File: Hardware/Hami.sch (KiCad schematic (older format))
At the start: 45 parts, among them J1 OLED, J2 BAT, SW1 Reset, SW10 MX, SW11 MX, SW12 MX, SW13 MX, SW14 MX, SW15 MX, SW16 MX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

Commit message: Hami V1.1
Because who doesn't need rotary encoder support in the botton and top left corners? Also re-routed some of the traces.
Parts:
- added SW20: Rot_1, Rotary_Encoder:RotaryEncoder_Alps_EC11E-Switch_Vertical_H20mm, symbol Device:Rotary_Encoder_Switch
- added SW21: Rot_2, Rotary_Encoder:RotaryEncoder_Alps_EC11E-Switch_Vertical_H20mm, symbol Device:Rotary_Encoder_Switch
- SW10, SW11, SW12, SW13, SW14, SW15, SW16, SW17, SW18, SW19, SW2, SW3, SW4, SW5, SW6, SW7, SW8, SW9: symbol Numpad:MX-NoLED -> Hami:MX-NoLED
- U1: symbol Numpad:ProMicro -> Hami:ProMicro
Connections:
- net labels added: Rot_1A, Rot_1B, Rot_2A, Rot_2B
- net labels removed: GND2
- wire segments 67 -> 76
- no-connect marks 7 -> 5
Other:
- moved on the sheet: D1, D10, D11, D12, D13, D14, D15, D16, D17, D18, D2, D3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

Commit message: Changed footprint references
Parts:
- J1: footprint Numpad:PinHeader_1x04_P2.54mm_Vertical_No_Silk -> Hami:PinHeader_1x04_P2.54mm_Vertical_No_Silk
- J2: footprint Numpad:Battery_Solder_Points -> Hami:Battery_Solder_Points
- SW10, SW11, SW12, SW13, SW14, SW15, SW16, SW17, SW2, SW3, SW4, SW5, SW6, SW7, SW8, SW9: footprint Numpad:CherryMX_Hotswap_SMK -> Hami:CherryMX_Hotswap_SMK
- SW18, SW19: footprint Numpad:CherryMX_Hotswap_2u_SMK -> Hami:CherryMX_Hotswap_2u_SMK
- U1: footprint Numpad:ArduinoProMicro_Blank -> Hami:ArduinoProMicro_Blank
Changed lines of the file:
@@
 F 0 "SW7" H 6625 1300 50  0000 C CNN
 F 1 "MX" H 6625 850 60  0001 C CNN
-F 2 "Numpad:CherryMX_Hotswap_SMK" H 6625 1150 60  0001 C CNN
+F 2 "Hami:CherryMX_Hotswap_SMK" H 6625 1150 60  0001 C CNN
 F 3 "" H 6625 1150 60  0001 C CNN
 	1    6625 1150
@@
 F 0 "SW12" H 7075 1300 50  0000 C CNN
 F 1 "MX" H 7075 850 60  0001 C CNN
-F 2 "Numpad:CherryMX_Hotswap_SMK" H 7075 1150 60  0001 C CNN
+F 2 "Hami:CherryMX_Hotswap_SMK" H 7075 1150 60  0001 C CNN
 F 3 "" H 7075 1150 60  0001 C CNN
 	1    7075 1150
@@
 F 0 "SW17" H 7575 1300 50  0000 C CNN
 F 1 "MX" H 7575 850 60  0001 C CNN
-F 2 "Numpad:CherryMX_Hotswap_SMK" H 7575 1150 60  0001 C CNN
+F 2 "Hami:CherryMX_Hotswap_SMK" H 7575 1150 60  0001 C CNN
 F 3 "" H 7575 1150 60  0001 C CNN
 	1    7575 1150
@@
 F 0 "SW8" H 6625 1900 50  0000 C CNN
 F 1 "MX" H 6625 1450 60  0001 C CNN
-F 2 "Numpad:CherryMX_Hotswap_SMK" H 6625 1750 60  0001 C CNN
+F 2 "Hami:CherryMX_Hotswap_SMK" H 6625 1750 60  0001 C CNN
 F 3 "" H 6625 1750 60  0001 C CNN
 	1    6625 1750
@@
 F 0 "SW13" H 7075 1900 50  0000 C CNN
 F 1 "MX" H 7075 1450 60  0001 C CNN
-F 2 "Numpad:CherryMX_Hotswap_SMK" H 7075 1750 60  0001 C CNN
+F 2 "Hami:CherryMX_Hotswap_SMK" H 7075 1750 60  0001 C CNN
 F 3 "" H 7075 1750 60  0001 C CNN
 	1    7075 1750
@@
 F 0 "SW9" H 6625 2500 50  0000 C CNN
 F 1 "MX" H 6625 2050 60  0001 C CNN
-F 2 "Numpad:CherryMX_Hotswap_SMK" H 6625 2350 60  0001 C CNN
+F 2 "Hami:CherryMX_Hotswap_SMK" H 6625 2350 60  0001 C CNN
 F 3 "" H 6625 2350 60  0001 C CNN
 	1    6625 2350
@@
 F 0 "SW14" H 7075 2500 50  0000 C CNN
 F 1 "MX" H 7075 2050 60  0001 C CNN
-F 2 "Numpad:CherryMX_Hotswap_SMK" H 7075 2350 60  0001 C CNN
+F 2 "Hami:CherryMX_Hotswap_SMK" H 7075 2350 60  0001 C CNN
 F 3 "" H 7075 2350 60  0001 C CNN
 	1    7075 2350
@@
 F 0 "SW10" H 6625 3100 50  0000 C CNN
 F 1 "MX" H 6625 2650 60  0001 C CNN
-F 2 "Numpad:CherryMX_Hotswap_SMK" H 6625 2950 60  0001 C CNN
+F 2 "Hami:CherryMX_Hotswap_SMK" H 6625 2950 60  0001 C CNN
 F 3 "" H 6625 2950 60  0001 C CNN
 	1    6625 2950
@@
 F 0 "SW15" H 7075 3100 50  0000 C CNN
 F 1 "MX" H 7075 2650 60  0001 C CNN
-F 2 "Numpad:CherryMX_Hotswap_SMK" H 7075 2950 60  0001 C CNN
+F 2 "Hami:CherryMX_Hotswap_SMK" H 7075 2950 60  0001 C CNN
 F 3 "" H 7075 2950 60  0001 C CNN
 	1    7075 2950
@@
 F 0 "SW16" H 7075 3700 50  0000 C CNN
 F 1 "MX" H 7075 3250 60  0001 C CNN
-F 2 "Numpad:CherryMX_Hotswap_SMK" H 7075 3550 60  0001 C CNN
+F 2 "Hami:CherryMX_Hotswap_SMK" H 7075 3550 60  0001 C CNN
 F 3 "" H 7075 3550 60  0001 C CNN
 	1    7075 3550
@@
 F 0 "SW18" H 7575 2500 50  0000 C CNN
 F 1 "MX" H 7575 2050 60  0001 C CNN
-F 2 "Numpad:CherryMX_Hotswap_2u_SMK" H 7575 2350 60  0001 C CNN
+F 2 "Hami:CherryMX_Hotswap_2u_SMK" H 7575 2350 60  0001 C CNN
 F 3 "" H 7575 2350 60  0001 C CNN
 	1    7575 2350
@@
 F 0 "SW19" H 7575 3700 50  0000 C CNN
 F 1 "MX" H 7575 3250 60  0001 C CNN
-F 2 "Numpad:CherryMX_Hotswap_2u_SMK" H 7575 3550 60  0001 C CNN
+F 2 "Hami:CherryMX_Hotswap_2u_SMK" H 7575 3550 60  0001 C CNN
 F 3 "" H 7575 3550 60  0001 C CNN
 	1    7575 3550
@@
 F 0 "SW2" H 6175 1300 50  0000 C CNN
 F 1 "MX" H 6175 850 60  0001 C CNN
-F 2 "Numpad:CherryMX_Hotswap_SMK" H 6175 1150 60  0001 C CNN
+F 2 "Hami:CherryMX_Hotswap_SMK" H 6175 1150 60  0001 C CNN
 F 3 "" H 6175 1150 60  0001 C CNN
 	1    6175 1150
@@
 F 0 "SW5" H 6175 3100 50  0000 C CNN
 F 1 "MX" H 6175 2650 60  0001 C CNN
-F 2 "Numpad:CherryMX_Hotswap_SMK" H 6175 2950 60  0001 C CNN
+F 2 "Hami:CherryMX_Hotswap_SMK" H 6175 2950 60  0001 C CNN
 F 3 "" H 6175 2950 60  0001 C CNN
 	1    6175 2950
@@
 F 0 "SW4" H 6175 2500 50  0000 C CNN
 F 1 "MX" H 6175 2050 60  0001 C CNN
-F 2 "Numpad:CherryMX_Hotswap_SMK" H 6175 2350 60  0001 C CNN
+F 2 "Hami:CherryMX_Hotswap_SMK" H 6175 2350 60  0001 C CNN
 F 3 "" H 6175 2350 60  0001 C CNN
 	1    6175 2350
@@
 F 0 "SW3" H 6175 1900 50  0000 C CNN
 F 1 "MX" H 6175 1450 60  0001 C CNN
-F 2 "Numpad:CherryMX_Hotswap_SMK" H 6175 1750 60  0001 C CNN
+F 2 "Hami:CherryMX_Hotswap_SMK" H 6175 1750 60  0001 C CNN
 F 3 "" H 6175 1750 60  0001 C CNN
 	1    6175 1750
@@
 F 0 "J2" H 3855 1342 50  0000 L CNN
 F 1 "BAT" H 3855 1251 50  0000 L CNN
-F 2 "Numpad:Battery_Solder_Points" H 3775 1350 50  0001 C CNN
+F 2 "Hami:Battery_Solder_Points" H 3775 1350 50  0001 C CNN
 F 3 "~" H 3775 1350 50  0001 C CNN
 	1    3775 1350
@@
 F 0 "SW6" H 6175 3700 50  0000 C CNN
 F 1 "MX" H 6175 3250 60  0001 C CNN
-F 2 "Numpad:CherryMX_Hotswap_SMK" H 6175 3550 60  0001 C CNN
+F 2 "Hami:CherryMX_Hotswap_SMK" H 6175 3550 60  0001 C CNN
 F 3 "" H 6175 3550 60  0001 C CNN
 	1    6175 3550
@@
 F 0 "SW11" H 6625 3700 50  0000 C CNN
 F 1 "MX" H 6625 3250 60  0001 C CNN
-F 2 "Numpad:CherryMX_Hotswap_SMK" H 6625 3550 60  0001 C CNN
+F 2 "Hami:CherryMX_Hotswap_SMK" H 6625 3550 60  0001 C CNN
 F 3 "" H 6625 3550 60  0001 C CNN
 	1    6625 3550
@@
 F 0 "J1" H 2918 2825 50  0000 C CNN
 F 1 "OLED" H 2918 2916 50  0000 C CNN
-F 2 "Numpad:PinHeader_1x04_P2.54mm_Vertical_No_Silk" H 3000 3250 50  0001 C CNN
+F 2 "Hami:PinHeader_1x04_P2.54mm_Vertical_No_Silk" H 3000 3250 50  0001 C CNN
 F 3 "~" H 3000 3250 50  0001 C CNN
 	1    3000 3250
@@
 F 0 "U1" H 2500 2737 60  0000 C CNN
 F 1 "ProMicro" H 2500 2631 60  0000 C CNN
-F 2 "Numpad:ArduinoProMicro_Blank" V 3550 -600 60  0001 C CNN
+F 2 "Hami:ArduinoProMicro_Blank" V 3550 -600 60  0001 C CNN
 F 3 "" V 3550 -600 60  0001 C CNN
 	1    2500 1900

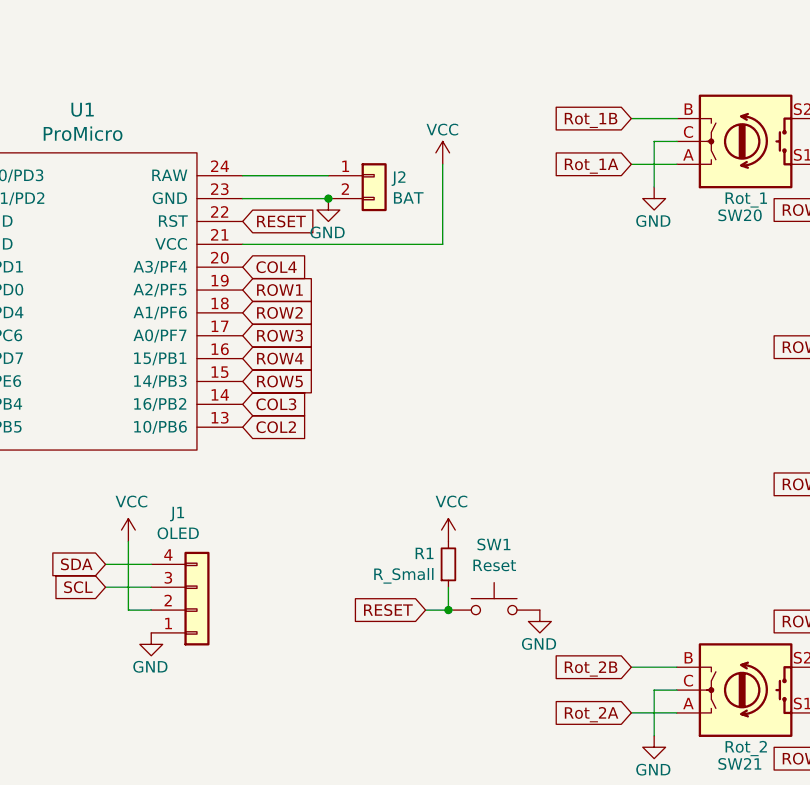
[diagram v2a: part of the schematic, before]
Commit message: Moved position of OLED, added new plate
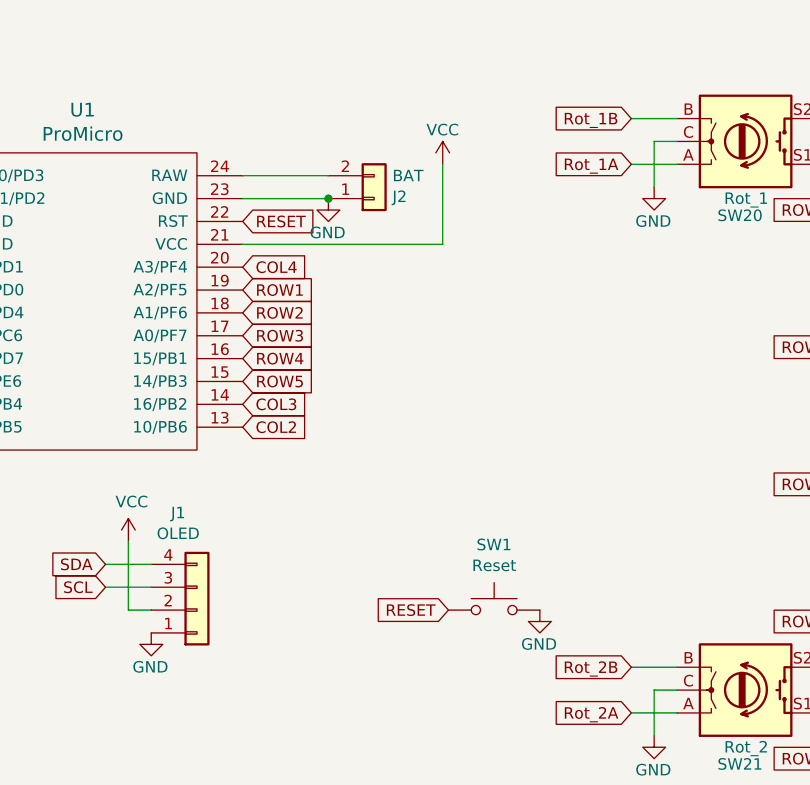
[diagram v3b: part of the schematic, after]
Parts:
- removed R1: R_Small, Resistor_SMD:R_0603_1608Metric, symbol Device:R_Small
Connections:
- net GND: now also J2.1 (Pin_1); no longer J2.2 (Pin_2)
- net at U1.24 (RAW): now also J2.2 (Pin_2); no longer J2.1 (Pin_1)
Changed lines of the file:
@@
 	-1   0    0    -1
-$EndComp
-Text GLabel 4000 3250 0    50   Input ~ 0
-RESET
-Wire Wire Line
-	4100 3250 4000 3250
-$Comp
-L Switch:SW_Push SW1
-U 1 1 5E7DD54D
-P 4300 3250
-F 0 "SW1" H 4300 3535 50  0000 C CNN
-F 1 "Reset" H 4300 3444 50  0000 C CNN
-F 2 "Button_Switch_SMD:SW_SPST_TL3342" H 4300 3450 50  0001 C CNN
-F 3 "~" H 4300 3450 50  0001 C CNN
-	1    4300 3250
-	1    0    0    -1
 $EndComp
 $Comp
@@
 Wire Wire Line
 	7125 3900 7625 3900
-$Comp
-L Device:R_Small R1
-U 1 1 5F74D470
-P 4100 3050
-F 0 "R1" H 4041 3004 50  0000 R CNN
-F 1 "R_Small" H 4041 3095 50  0000 R CNN
-F 2 "Resistor_SMD:R_0603_1608Metric" H 4100 3050 50  0001 C CNN
-F 3 "~" H 4100 3050 50  0001 C CNN
-	1    4100 3050
-	1    0    0    1
-$EndComp
-Wire Wire Line
-	4100 3150 4100 3250
-Connection ~ 4100 3250
-$Comp
-L power:VCC #PWR0102
-U 1 1 5F7A076F
-P 4100 2950
-F 0 "#PWR0102" H 4100 2800 50  0001 C CNN
-F 1 "VCC" H 4115 3123 50  0000 C CNN
-F 2 "" H 4100 2950 50  0001 C CNN
-F 3 "" H 4100 2950 50  0001 C CNN
-	1    4100 2950
-	1    0    0    -1
-$EndComp
-Text GLabel 3200 1850 2    50   Input ~ 0
-ROW1
-Text GLabel 3200 2050 2    50   Input ~ 0
-ROW3
-Text GLabel 3200 2150 2    50   Input ~ 0
-ROW4
-Text GLabel 3200 2250 2    50   Input ~ 0
-ROW5
-Text GLabel 3200 1950 2    50   Input ~ 0
-ROW2
-Text GLabel 3200 1750 2    50   Input ~ 0
-COL4
-Text GLabel 3200 2450 2    50   Input ~ 0
-COL2
-Text GLabel 1800 2450 0    50   Input ~ 0
-COL1
-Text GLabel 3200 2350 2    50   Input ~ 0
-COL3
 Wire Wire Line
 	6225 3900 6675 3900
@@
 F 3 "" H 4075 1300 50  0001 C CNN
 	1    4075 1300
-	1    0    0    -1
-$EndComp
-$Comp
-L Connector_Generic:Conn_01x02 J2
-U 1 1 5F95AA4D
-P 3775 1350
-F 0 "J2" H 3855 1342 50  0000 L CNN
-F 1 "BAT" H 3855 1251 50  0000 L CNN
-F 2 "Hami:Battery_Solder_Points" H 3775 1350 50  0001 C CNN
-F 3 "~" H 3775 1350 50  0001 C CNN
-	1    3775 1350
 	1    0    0    -1
 $EndComp
@@
 Text GLabel 1800 1750 0    50   Input ~ 0
 SDA
-NoConn ~ 1800 1950
-NoConn ~ 1800 1450
-NoConn ~ 1800 1350
 $Comp
 L power:GND #PWR0105
@@
 Wire Wire Line
 	3575 1450 3200 1450
-Connection ~ 3575 1450
 Wire Wire Line
 	3200 1350 3575 1350
@@
 Wire Wire Line
 	5000 1200 5100 1200
+Text GLabel 4900 1300 0    50   Input ~ 0
+Rot_1A
+Text GLabel 4900 1100 0    50   Input ~ 0
+Rot_1B
+Wire Wire Line
+	4900 1300 5100 1300
+Wire Wire Line
+	5100 1100 4900 1100
+Text GLabel 4900 3700 0    50   Input ~ 0
+Rot_2A
+Text GLabel 4900 3500 0    50   Input ~ 0
+Rot_2B
+Wire Wire Line
+	4900 3500 5100 3500
+Wire Wire Line
+	4900 3700 5100 3700
+$Comp
+L power:GND #PWR0101
+U 1 1 5F7C7BC9
+P 2800 3350
+F 0 "#PWR0101" H 2800 3100 50  0001 C CNN
+F 1 "GND" H 2875 3200 50  0000 R CNN
+F 2 "" H 2800 3350 50  0001 C CNN
+F 3 "" H 2800 3350 50  0001 C CNN
+	1    2800 3350
+	1    0    0    -1
+$EndComp
+$Comp
+L Hami:ProMicro U1
+U 1 1 5D85EAF7
+P 2500 1900
+F 0 "U1" H 2500 2737 60  0000 C CNN
+F 1 "ProMicro" H 2500 2631 60  0000 C CNN
+F 2 "Hami:ArduinoProMicro_Blank" V 3550 -600 60  0001 C CNN
+F 3 "" V 3550 -600 60  0001 C CNN
+	1    2500 1900
+	1    0    0    -1
+$EndComp
+$Comp
+L Switch:SW_Push SW1
+U 1 1 5E7DD54D
+P 4300 3250
+F 0 "SW1" H 4300 3535 50  0000 C CNN
+F 1 "Reset" H 4300 3444 50  0000 C CNN
+F 2 "Button_Switch_SMD:SW_SPST_TL3342" H 4300 3450 50  0001 C CNN
+F 3 "~" H 4300 3450 50  0001 C CNN
+	1    4300 3250
+	1    0    0    -1
+$EndComp
+Text GLabel 4100 3250 0    50   Input ~ 0
+RESET
 $Comp
 L power:GND #PWR0107
@@
 	1    0    0    -1
 $EndComp
-Text GLabel 4900 1300 0    50   Input ~ 0
-Rot_1A
-Text GLabel 4900 1100 0    50   Input ~ 0
-Rot_1B
-Wire Wire Line
-	4900 1300 5100 1300
-Wire Wire Line
-	5100 1100 4900 1100
-Text GLabel 4900 3700 0    50   Input ~ 0
-Rot_2A
-Text GLabel 4900 3500 0    50   Input ~ 0
-Rot_2B
-Wire Wire Line
-	4900 3500 5100 3500
-Wire Wire Line
-	4900 3700 5100 3700
-$Comp
-L Hami:ProMicro U1
-U 1 1 5D85EAF7
-P 2500 1900
-F 0 "U1" H 2500 2737 60  0000 C CNN
-F 1 "ProMicro" H 2500 2631 60  0000 C CNN
-F 2 "Hami:ArduinoProMicro_Blank" V 3550 -600 60  0001 C CNN
-F 3 "" V 3550 -600 60  0001 C CNN
-	1    2500 1900
-	1    0    0    -1
-$EndComp
-NoConn ~ 1800 1650
-NoConn ~ 1800 1550
-$Comp
-L power:GND #PWR0101
-U 1 1 5F7C7BC9
-P 2800 3350
-F 0 "#PWR0101" H 2800 3100 50  0001 C CNN
-F 1 "GND" H 2875 3200 50  0000 R CNN
-F 2 "" H 2800 3350 50  0001 C CNN
-F 3 "" H 2800 3350 50  0001 C CNN
-	1    2800 3350
-	1    0    0    -1
-$EndComp
-Text GLabel 1800 2350 0    50   Input ~ 0
-Rot_1B
-Text GLabel 1800 2250 0    50   Input ~ 0
-Rot_1A
-Text GLabel 1800 2150 0    50   Input ~ 0
-Rot_2B
-Text GLabel 1800 2050 0    50   Input ~ 0
-Rot_2A
-$Comp
-L power:GND #PWR?
+$Comp
+L power:GND #PWR0106
 U 1 1 5F7F8187
 P 5000 3800
-F 0 "#PWR?" H 5000 3550 50  0001 C CNN
+F 0 "#PWR0106" H 5000 3550 50  0001 C CNN
 F 1 "GND" H 5075 3650 50  0000 R CNN
 F 2 "" H 5000 3800 50  0001 C CNN
@@
 $EndComp
 $Comp
-L power:GND #PWR?
+L power:GND #PWR0108
 U 1 1 5F7F8606
 P 5000 1400
-F 0 "#PWR?" H 5000 1150 50  0001 C CNN
+F 0 "#PWR0108" H 5000 1150 50  0001 C CNN
 F 1 "GND" H 5075 1250 50  0000 R CNN
 F 2 "" H 5000 1400 50  0001 C CNN
@@
 	1    0    0    -1
 $EndComp
+Text GLabel 1800 2450 0    50   Input ~ 0
+COL1
+NoConn ~ 1800 1950
+NoConn ~ 1800 1650
+NoConn ~ 1800 1550
+NoConn ~ 1800 1450
+NoConn ~ 1800 1350
+Text GLabel 3200 2350 2    50   Input ~ 0
+COL3
+Text GLabel 3200 2450 2    50   Input ~ 0
+COL2
+Text GLabel 3200 1750 2    50   Input ~ 0
+COL4
+Text GLabel 3200 1950 2    50   Input ~ 0
+ROW2
+Text GLabel 3200 2250 2    50   Input ~ 0
+ROW5
+Text GLabel 3200 2150 2    50   Input ~ 0
+ROW4
+Text GLabel 3200 2050 2    50   Input ~ 0
+ROW3
+Text GLabel 3200 1850 2    50   Input ~ 0
+ROW1
+$Comp
+L Connector_Generic:Conn_01x02 J2
+U 1 1 5F95AA4D
+P 3775 1450
+F 0 "J2" H 3855 1442 50  0000 L CNN
+F 1 "BAT" H 3855 1351 50  0000 L CNN
+F 2 "Hami:Battery_Solder_Points" H 3775 1450 50  0001 C CNN
+F 3 "~" H 3775 1450 50  0001 C CNN
+	1    3775 1450
+	1    0    0    1
+$EndComp
+Connection ~ 3575 1450
+Text GLabel 1800 2050 0    50   Input ~ 0
+Rot_2A
+Text GLabel 1800 2150 0    50   Input ~ 0
+Rot_2B
+Text GLabel 1800 2250 0    50   Input ~ 0
+Rot_1A
+Text GLabel 1800 2350 0    50   Input ~ 0
+Rot_1B
 $EndSCHEMATC
